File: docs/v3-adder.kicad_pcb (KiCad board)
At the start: 2 copper layers, 19 x 111.5 mm, 101 parts, among them J1 Thonkiconn, J2 Thonkiconn, J3 Thonkiconn, J4 Thonkiconn, J5 Thonkiconn, J6 Thonkiconn, J7 Thonkiconn, J8 Thonkiconn, P1 Eurorack 2x5, SW1 200-MSP3 (SPDT ON-OFF-ON), SW2 200-MSP3 (SPDT ON-OFF-ON), SW3 200-MSP3 (SPDT ON-OFF-ON), SW4 200-MSP3 (SPDT ON-OFF-ON), SW5 200-MSP1 (SPDT ON-ON), SW6 200-MDP6 (DPDT ON-ON-ON), SW7 200-MDP6 (DPDT ON-ON-ON), SW8 200-MDP6 (DPDT ON-ON-ON), U1 OPA4196, U2 OPA4196, U3 OPA4196, U4 L78L05, U5 L79L05

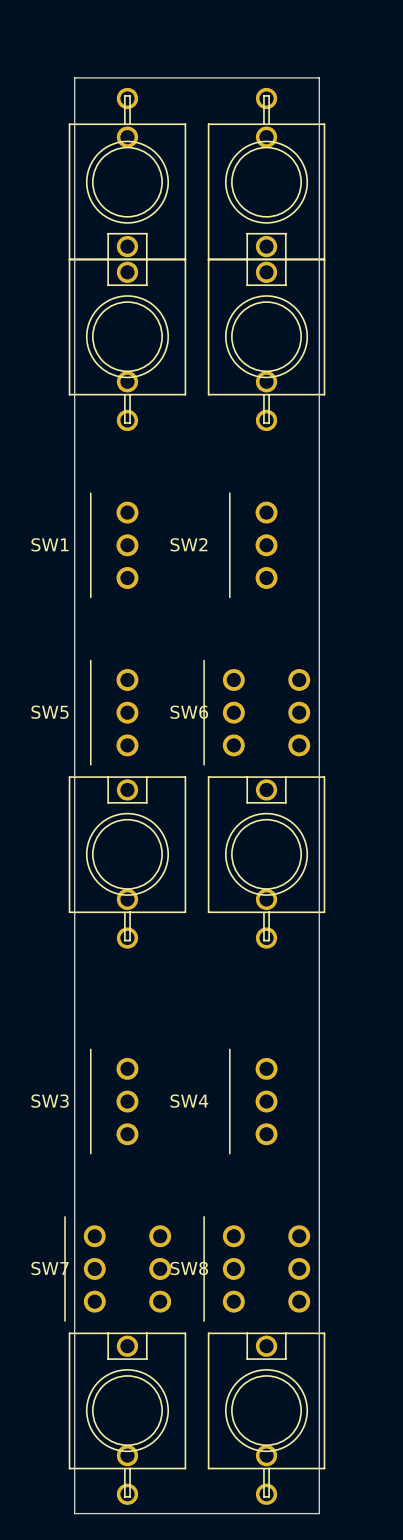
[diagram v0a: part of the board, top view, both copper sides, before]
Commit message: Narrow the column pitch to 10.4 so part bodies clear the board edge
The DPDT selector is 9.10 mm wide once rotated for a vertical throw, so two of
them occupy 18.2 mm of a 20 mm panel - 1.8 mm of slack for everything else. At
the old 10.8 pitch their bodies, and the 9.00 mm jack bodies, overhung a 19 mm
PCB by about 0.45 mm a side.

The fix trades against panel legibility, because the detent mark sits between a
toggle nut and its box edge, and moving a column inward closes that gap:

  pitch 10.8   marks 0.25 mm   board must be 19.90 mm
  pitch 10.6   marks 0.20 mm   board must be 19.70 mm
  pitch 10.4   marks 0.15 mm   board must be 19.50 mm
  pitch 10.0   marks 0.05 mm   - unmanufacturable

10.4 is the balance point: 19.5 mm is an ordinary 4 HP board width where 19.9
is at the limit, and 0.15 mm is the usual fab silkscreen minimum. My first
attempt went to 10.0 on a mistaken reading - I had measured the channel between
the two nuts rather than the nut-to-box strip the marks actually live in, and
the panel's own clearance check caught it at 0.05 mm.

Board is now 19.6 x 111.5 mm with every body inside it, the sixteen
panel-defined parts re-placed on the new columns, and the README hole schedule
and clearance figures brought up to date.

Panel DRC 0 violations, schematic ERC 0 errors 0 warnings, and the board's
silk_edge_clearance warnings are gone.

Co-Authored-By: Claude Opus 5 <noreply@anthropic.com>
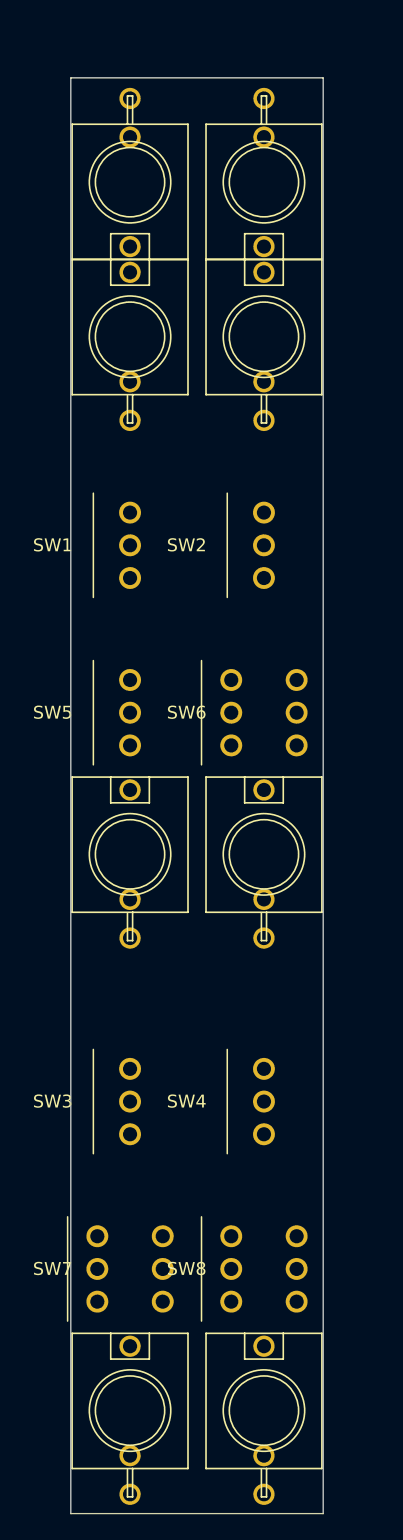
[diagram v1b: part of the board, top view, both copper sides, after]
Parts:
- moved J2 0.20 mm to (15.2, 16.6)
- moved J4 0.20 mm to (15.2, 28.6)
- moved J6 0.20 mm to (15.2, 68.8)
- moved J8 0.20 mm to (15.2, 112.0)
- moved SW2 0.20 mm to (15.2, 44.8)
- moved SW4 0.20 mm to (15.2, 88.0)
- moved SW6 0.20 mm to (15.2, 57.8)
- moved SW8 0.20 mm to (15.2, 101.0)
- moved J1 0.20 mm to (4.80, 16.6)
- moved J3 0.20 mm to (4.80, 28.6)
- moved J5 0.20 mm to (4.80, 68.8)
- moved J7 0.20 mm to (4.80, 112.0)
- moved SW1 0.20 mm to (4.80, 44.8)
- moved SW3 0.20 mm to (4.80, 88.0)
- moved SW5 0.20 mm to (4.80, 57.8)
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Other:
- board size 19 x 111.5 mm -> 19.6 x 111.5 mm
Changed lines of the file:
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@@
 	(footprint "eurorack:SW_Taiway_200_SPDT"
 		(layer "F.Cu")
-		(at 15.4 88.0 90)
+		(at 15.2 88.0 90)
 		(descr "Taiway series 200 sub-miniature SPDT toggle, PCB vertical, M2 PC thru-hole. Fits any 200-MSPx: ON-ON (MSP1), ON-OFF-ON (MSP3), and the momentary variants. Three terminals in a line on 2.54, 10-48 UNS bushing (o4.80 thread, 5.50 high, flat) -> o4.95 panel hole. Body 5.10 (throw axis, X) x 8.10. Pads numbered as the datasheet does: 1 and 3 are the throws, PAD 2 IS THE COMMON and is the centre terminal. Taiway's contact table reads 2-3 / OPEN / 2-1 in this numbering. Shares the throw axis and bushing with SW_Taiway_200_DPDT, so an SPDT and a DPDT sit on the same panel pitch.")
 		(tags "toggle switch spdt on-on on-off-on subminiature taiway 200 eurorack")
@@
 	(footprint "eurorack:Thonkiconn_PJ301M"
 		(layer "F.Cu")
-		(at 15.4 28.6)
+		(at 15.2 28.6)
 		(property "Reference" "J4"
 			(at -4.7498 5.1054 270)
@@
 	(footprint "eurorack:SW_Taiway_200_SPDT"
 		(layer "F.Cu")
-		(at 4.6 88.0 90)
+		(at 4.8 88.0 90)
 		(descr "Taiway series 200 sub-miniature SPDT toggle, PCB vertical, M2 PC thru-hole. Fits any 200-MSPx: ON-ON (MSP1), ON-OFF-ON (MSP3), and the momentary variants. Three terminals in a line on 2.54, 10-48 UNS bushing (o4.80 thread, 5.50 high, flat) -> o4.95 panel hole. Body 5.10 (throw axis, X) x 8.10. Pads numbered as the datasheet does: 1 and 3 are the throws, PAD 2 IS THE COMMON and is the centre terminal. Taiway's contact table reads 2-3 / OPEN / 2-1 in this numbering. Shares the throw axis and bushing with SW_Taiway_200_DPDT, so an SPDT and a DPDT sit on the same panel pitch.")
 		(tags "toggle switch spdt on-on on-off-on subminiature taiway 200 eurorack")
@@
 	(footprint "eurorack:Thonkiconn_PJ301M"
 		(layer "F.Cu")
-		(at 15.4 16.6 180)
+		(at 15.2 16.6 180)
 		(property "Reference" "J2"
 			(at -4.7498 5.1054 270)
@@
 	(footprint "eurorack:SW_Taiway_200_DPDT"
 		(layer "F.Cu")
-		(at 4.6 101.0 90)
+		(at 4.8 101.0 90)
 		(descr "Taiway series 200 sub-miniature DPDT toggle, PCB vertical, M2 PC thru-hole. Fits any 200-MDPx: ON-ON, ON-OFF-ON, or the custom MDP6 ON-ON-ON. Terminals on a 2.54 x 5.08 grid, 10-48 UNS bushing (o4.80 thread, 5.50 high, flat) -> o4.95 panel hole. Body 8.10 (throw axis, X) x 9.10. PADS ARE NUMBERED AS THE DATASHEET DOES: pins 1-2-3 are one pole and 4-5-6 the other, with the COMMONS on 2 and 5, i.e. the centre of each row. Taiway's contact table is written in this numbering (ON-ON-ON reads 2-3,5-6 / 2-3,5-4 / 2-1,5-4), so a symbol drawn from the datasheet drops straight on. NOTE the sibling SW_200_MDP3_DPDT in this library is the same physical part with a deliberately different remap, commons on pads 1 and 4, for symbols numbered that way - the two are NOT interchangeable. Pick whichever matches your symbol and check the common lands on a centre terminal.")
 		(tags "toggle switch dpdt on-on-on on-off-on subminiature taiway 200 eurorack")
@@
 	(footprint "eurorack:SW_Taiway_200_SPDT"
 		(layer "F.Cu")
-		(at 4.6 57.8 90)
+		(at 4.8 57.8 90)
 		(descr "Taiway series 200 sub-miniature SPDT toggle, PCB vertical, M2 PC thru-hole. Fits any 200-MSPx: ON-ON (MSP1), ON-OFF-ON (MSP3), and the momentary variants. Three terminals in a line on 2.54, 10-48 UNS bushing (o4.80 thread, 5.50 high, flat) -> o4.95 panel hole. Body 5.10 (throw axis, X) x 8.10. Pads numbered as the datasheet does: 1 and 3 are the throws, PAD 2 IS THE COMMON and is the centre terminal. Taiway's contact table reads 2-3 / OPEN / 2-1 in this numbering. Shares the throw axis and bushing with SW_Taiway_200_DPDT, so an SPDT and a DPDT sit on the same panel pitch.")
 		(tags "toggle switch spdt on-on on-off-on subminiature taiway 200 eurorack")
@@
 	(footprint "eurorack:Thonkiconn_PJ301M"
 		(layer "F.Cu")
-		(at 4.6 112.0)
+		(at 4.8 112.0)
 		(property "Reference" "J7"
 			(at -4.7498 5.1054 270)
@@
 	(footprint "eurorack:SW_Taiway_200_DPDT"
 		(layer "F.Cu")
-		(at 15.4 101.0 90)
+		(at 15.2 101.0 90)
 		(descr "Taiway series 200 sub-miniature DPDT toggle, PCB vertical, M2 PC thru-hole. Fits any 200-MDPx: ON-ON, ON-OFF-ON, or the custom MDP6 ON-ON-ON. Terminals on a 2.54 x 5.08 grid, 10-48 UNS bushing (o4.80 thread, 5.50 high, flat) -> o4.95 panel hole. Body 8.10 (throw axis, X) x 9.10. PADS ARE NUMBERED AS THE DATASHEET DOES: pins 1-2-3 are one pole and 4-5-6 the other, with the COMMONS on 2 and 5, i.e. the centre of each row. Taiway's contact table is written in this numbering (ON-ON-ON reads 2-3,5-6 / 2-3,5-4 / 2-1,5-4), so a symbol drawn from the datasheet drops straight on. NOTE the sibling SW_200_MDP3_DPDT in this library is the same physical part with a deliberately different remap, commons on pads 1 and 4, for symbols numbered that way - the two are NOT interchangeable. Pick whichever matches your symbol and check the common lands on a centre terminal.")
 		(tags "toggle switch dpdt on-on-on on-off-on subminiature taiway 200 eurorack")
@@
 	(footprint "eurorack:Thonkiconn_PJ301M"
 		(layer "F.Cu")
-		(at 4.6 68.8)
+		(at 4.8 68.8)
 		(property "Reference" "J5"
 			(at -4.7498 5.1054 270)
@@
 	(footprint "eurorack:SW_Taiway_200_DPDT"
 		(layer "F.Cu")
-		(at 15.4 57.8 90)
+		(at 15.2 57.8 90)
 		(descr "Taiway series 200 sub-miniature DPDT toggle, PCB vertical, M2 PC thru-hole. Fits any 200-MDPx: ON-ON, ON-OFF-ON, or the custom MDP6 ON-ON-ON. Terminals on a 2.54 x 5.08 grid, 10-48 UNS bushing (o4.80 thread, 5.50 high, flat) -> o4.95 panel hole. Body 8.10 (throw axis, X) x 9.10. PADS ARE NUMBERED AS THE DATASHEET DOES: pins 1-2-3 are one pole and 4-5-6 the other, with the COMMONS on 2 and 5, i.e. the centre of each row. Taiway's contact table is written in this numbering (ON-ON-ON reads 2-3,5-6 / 2-3,5-4 / 2-1,5-4), so a symbol drawn from the datasheet drops straight on. NOTE the sibling SW_200_MDP3_DPDT in this library is the same physical part with a deliberately different remap, commons on pads 1 and 4, for symbols numbered that way - the two are NOT interchangeable. Pick whichever matches your symbol and check the common lands on a centre terminal.")
 		(tags "toggle switch dpdt on-on-on on-off-on subminiature taiway 200 eurorack")
@@
 	(footprint "eurorack:Thonkiconn_PJ301M"
 		(layer "F.Cu")
-		(at 4.6 28.6)
+		(at 4.8 28.6)
 		(property "Reference" "J3"
 			(at -4.7498 5.1054 270)
@@
 	(footprint "eurorack:Thonkiconn_PJ301M"
 		(layer "F.Cu")
-		(at 4.6 16.6 180)
+		(at 4.8 16.6 180)
 		(property "Reference" "J1"
 			(at -4.7498 5.1054 270)
@@
 	(footprint "eurorack:Thonkiconn_PJ301M"
 		(layer "F.Cu")
-		(at 15.4 68.8)
+		(at 15.2 68.8)
 		(property "Reference" "J6"
 			(at -4.7498 5.1054 270)
@@
 	(footprint "eurorack:Thonkiconn_PJ301M"
 		(layer "F.Cu")
-		(at 15.4 112.0)
+		(at 15.2 112.0)
 		(property "Reference" "J8"
 			(at -4.7498 5.1054 270)
@@
 	(footprint "eurorack:SW_Taiway_200_SPDT"
 		(layer "F.Cu")
-		(at 15.4 44.8 90)
+		(at 15.2 44.8 90)
 		(descr "Taiway series 200 sub-miniature SPDT toggle, PCB vertical, M2 PC thru-hole. Fits any 200-MSPx: ON-ON (MSP1), ON-OFF-ON (MSP3), and the momentary variants. Three terminals in a line on 2.54, 10-48 UNS bushing (o4.80 thread, 5.50 high, flat) -> o4.95 panel hole. Body 5.10 (throw axis, X) x 8.10. Pads numbered as the datasheet does: 1 and 3 are the throws, PAD 2 IS THE COMMON and is the centre terminal. Taiway's contact table reads 2-3 / OPEN / 2-1 in this numbering. Shares the throw axis and bushing with SW_Taiway_200_DPDT, so an SPDT and a DPDT sit on the same panel pitch.")
 		(tags "toggle switch spdt on-on on-off-on subminiature taiway 200 eurorack")
@@
 	(footprint "eurorack:SW_Taiway_200_SPDT"
 		(layer "F.Cu")
-		(at 4.6 44.8 90)
+		(at 4.8 44.8 90)
 		(descr "Taiway series 200 sub-miniature SPDT toggle, PCB vertical, M2 PC thru-hole. Fits any 200-MSPx: ON-ON (MSP1), ON-OFF-ON (MSP3), and the momentary variants. Three terminals in a line on 2.54, 10-48 UNS bushing (o4.80 thread, 5.50 high, flat) -> o4.95 panel hole. Body 5.10 (throw axis, X) x 8.10. Pads numbered as the datasheet does: 1 and 3 are the throws, PAD 2 IS THE COMMON and is the centre terminal. Taiway's contact table reads 2-3 / OPEN / 2-1 in this numbering. Shares the throw axis and bushing with SW_Taiway_200_DPDT, so an SPDT and a DPDT sit on the same panel pitch.")
 		(tags "toggle switch spdt on-on on-off-on subminiature taiway 200 eurorack")
@@
 	(embedded_fonts no)
 	(gr_line
-		(start 0.5 8.5)
-		(end 19.5 8.5)
+		(start 0.2 8.5)
+		(end 19.8 8.5)
 		(stroke
 			(width 0.1)
@@
 	)
 	(gr_line
-		(start 19.5 8.5)
-		(end 19.5 120.0)
+		(start 19.8 8.5)
+		(end 19.8 120.0)
 		(stroke
 			(width 0.1)
@@
 	)
 	(gr_line
-		(start 19.5 120.0)
-		(end 0.5 120.0)
+		(start 19.8 120.0)
+		(end 0.2 120.0)
 		(stroke
 			(width 0.1)
@@
 	)
 	(gr_line
-		(start 0.5 120.0)
-		(end 0.5 8.5)
+		(start 0.2 120.0)
+		(end 0.2 8.5)
 		(stroke
 			(width 0.1)
